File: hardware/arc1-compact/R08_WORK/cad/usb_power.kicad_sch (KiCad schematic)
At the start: 18 parts, among them J1 USB-C receptacle, U1 TUSB320LAI, U2 TPD2EUSB30

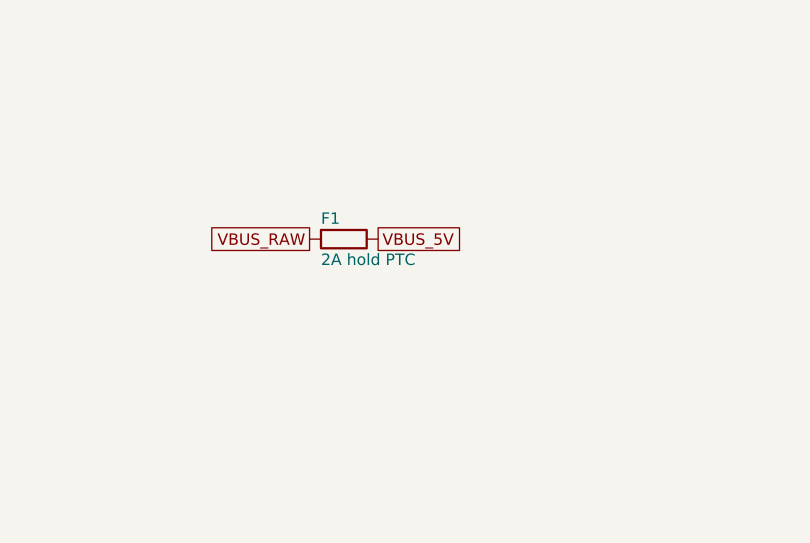
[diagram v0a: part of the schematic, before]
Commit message: ARC-1 Compact R08: rule checker + negative tests, margin analysis, diagnostic boot0 image, runner, dossiers, ledger, risk register, status
Co-Authored-By: Claude Opus 5.5 <noreply@anthropic.com>
Claude-Session: https://claude.ai/code/session_01UkiuLdbjDvK75uDzAPKsGs
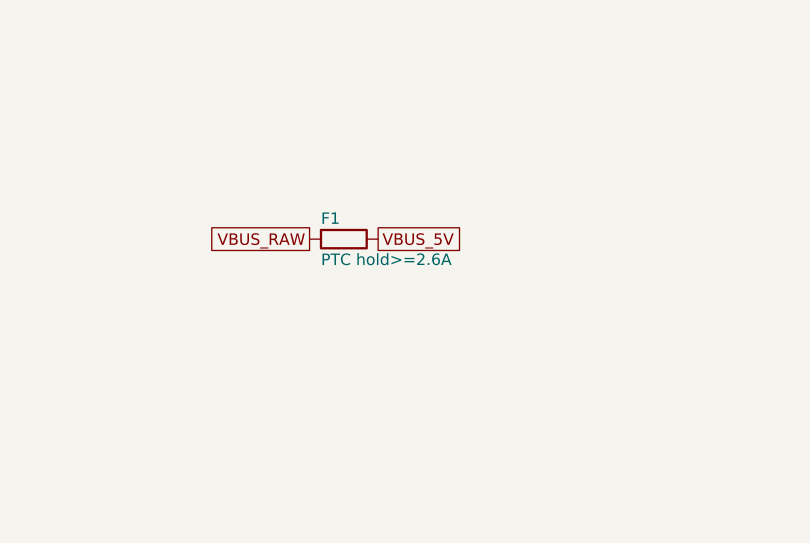
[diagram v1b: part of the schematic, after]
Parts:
- C1, C2, C3, R1, R2, R3, R4, R5, R6, R7: Evidence VERIFIED_BY_VENDOR_DOC -> GENERIC_PASSIVE (value from design.py / analysis; MPN only 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
- F1: value 2A hold PTC -> PTC hold>=2.6A; footprint Fuse:Fuse_1206_3216Metric -> Fuse:Fuse_1812_4532Metric; symbol ARC1_R08:F1206 -> ARC1_R08:F1812; Evidence VERIFIED_BY_VENDOR_DOC -> GENERIC_PASSIVE (value from design.py / analysis; MPN only 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; MPN 1206L200SLYR -> TBD (1812 PTC, hold >= 2.6 A, 6 V); Manufacturer Littelfuse -> TBD; Note CANDIDATE: hold current vs worst-case budget in POWER_TREE_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 -> hold current from the VBUS budget (analysis/electrical_marg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
- TP1, TP2, TP3: Evidence VERIFIED_BY_VENDOR_DOC -> GENERIC (no device-specific claim)
